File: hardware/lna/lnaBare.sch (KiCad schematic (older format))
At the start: 12 parts, among them J1 142-0701-801, J2 142-0701-801, J3 Conn_01x01_Male, U1 BGU8009

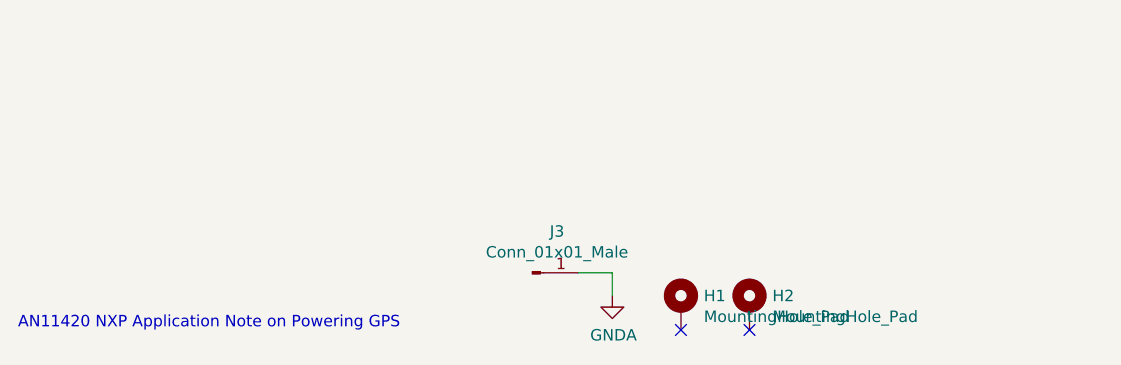
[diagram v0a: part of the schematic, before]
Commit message: added development board
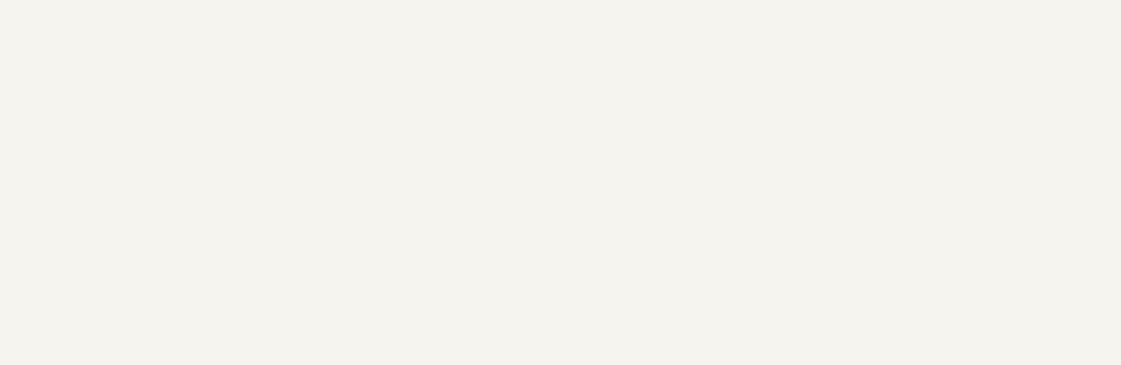
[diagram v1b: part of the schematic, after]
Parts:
- removed H1, H2: MountingHole_Pad, MountingHole:MountingHole_3.2mm_M3_Pad_Via, symbol Mechanical:MountingHole_Pad
- removed J3: Conn_01x01_Male, RF_Shielding:Laird_Technologies_BMI-S-101_13.66x12.70mm, symbol Connector:Conn_01x01_Male
- D1: footprint Diode_SMD:D_0402_1005Metric -> lna:SOIC-2
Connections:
- no-connect marks 2 -> 0
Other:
- note removed: "AN11420 NXP Application Note on Powering GPS\n"
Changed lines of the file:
@@
 EESchema Schematic File Version 4
-LIBS:lna-cache
+LIBS:lnaBare-cache
 EELAYER 30 0
 EELAYER END
@@
 	-1   0    0    -1
 $EndComp
-Text Notes 1300 7400 0    50   ~ 0
-AN11420 NXP Application Note on Powering GPS\n
 Wire Wire Line
 	3700 3600 3400 3600
@@
 F 0 "D1" V 5929 4253 50  0000 L CNN
 F 1 "Bi_ESD_Diode" V 6020 4253 50  0000 L CNN
-F 2 "Diode_SMD:D_0402_1005Metric" H 6000 4150 50  0001 C CNN
+F 2 "lna:SOIC-2" H 6000 4150 50  0001 C CNN
 F 3 "" H 6000 4150 50  0001 C CNN
 	1    6000 4150
@@
 $EndComp
 $Comp
-L Connector:Conn_01x01_Male J3
-U 1 1 5D6F996D
-P 3550 7150
-F 0 "J3" H 3658 7331 50  0000 C CNN
-F 1 "Conn_01x01_Male" H 3658 7240 50  0000 C CNN
-F 2 "RF_Shielding:Laird_Technologies_BMI-S-101_13.66x12.70mm" H 3550 7150 50  0001 C CNN
-F 3 "~" H 3550 7150 50  0001 C CNN
-	1    3550 7150
-	1    0    0    -1
-$EndComp
-$Comp
-L power:GNDA #PWR0104
-U 1 1 5D6F2F18
-P 3900 7250
-F 0 "#PWR0104" H 3900 7000 50  0001 C CNN
-F 1 "GNDA" H 3905 7077 50  0000 C CNN
-F 2 "" H 3900 7250 50  0001 C CNN
-F 3 "" H 3900 7250 50  0001 C CNN
-	1    3900 7250
-	1    0    0    -1
-$EndComp
-Wire Wire Line
-	3750 7150 3900 7150
-Wire Wire Line
-	3900 7150 3900 7250
-$Comp
-L Mechanical:MountingHole_Pad H1
-U 1 1 5D70E3CC
-P 4200 7300
-F 0 "H1" H 4300 7349 50  0000 L CNN
-F 1 "MountingHole_Pad" H 4300 7258 50  0000 L CNN
-F 2 "MountingHole:MountingHole_3.2mm_M3_Pad_Via" H 4200 7300 50  0001 C CNN
-F 3 "~" H 4200 7300 50  0001 C CNN
-	1    4200 7300
-	1    0    0    -1
-$EndComp
-$Comp
-L Mechanical:MountingHole_Pad H2
-U 1 1 5D70EDF1
-P 4500 7300
-F 0 "H2" H 4600 7349 50  0000 L CNN
-F 1 "MountingHole_Pad" H 4600 7258 50  0000 L CNN
-F 2 "MountingHole:MountingHole_3.2mm_M3_Pad_Via" H 4500 7300 50  0001 C CNN
-F 3 "~" H 4500 7300 50  0001 C CNN
-	1    4500 7300
-	1    0    0    -1
-$EndComp
-NoConn ~ 4200 7400
-NoConn ~ 4500 7400
-$Comp
 L Device:LED D2
